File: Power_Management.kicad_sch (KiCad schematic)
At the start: 21 parts

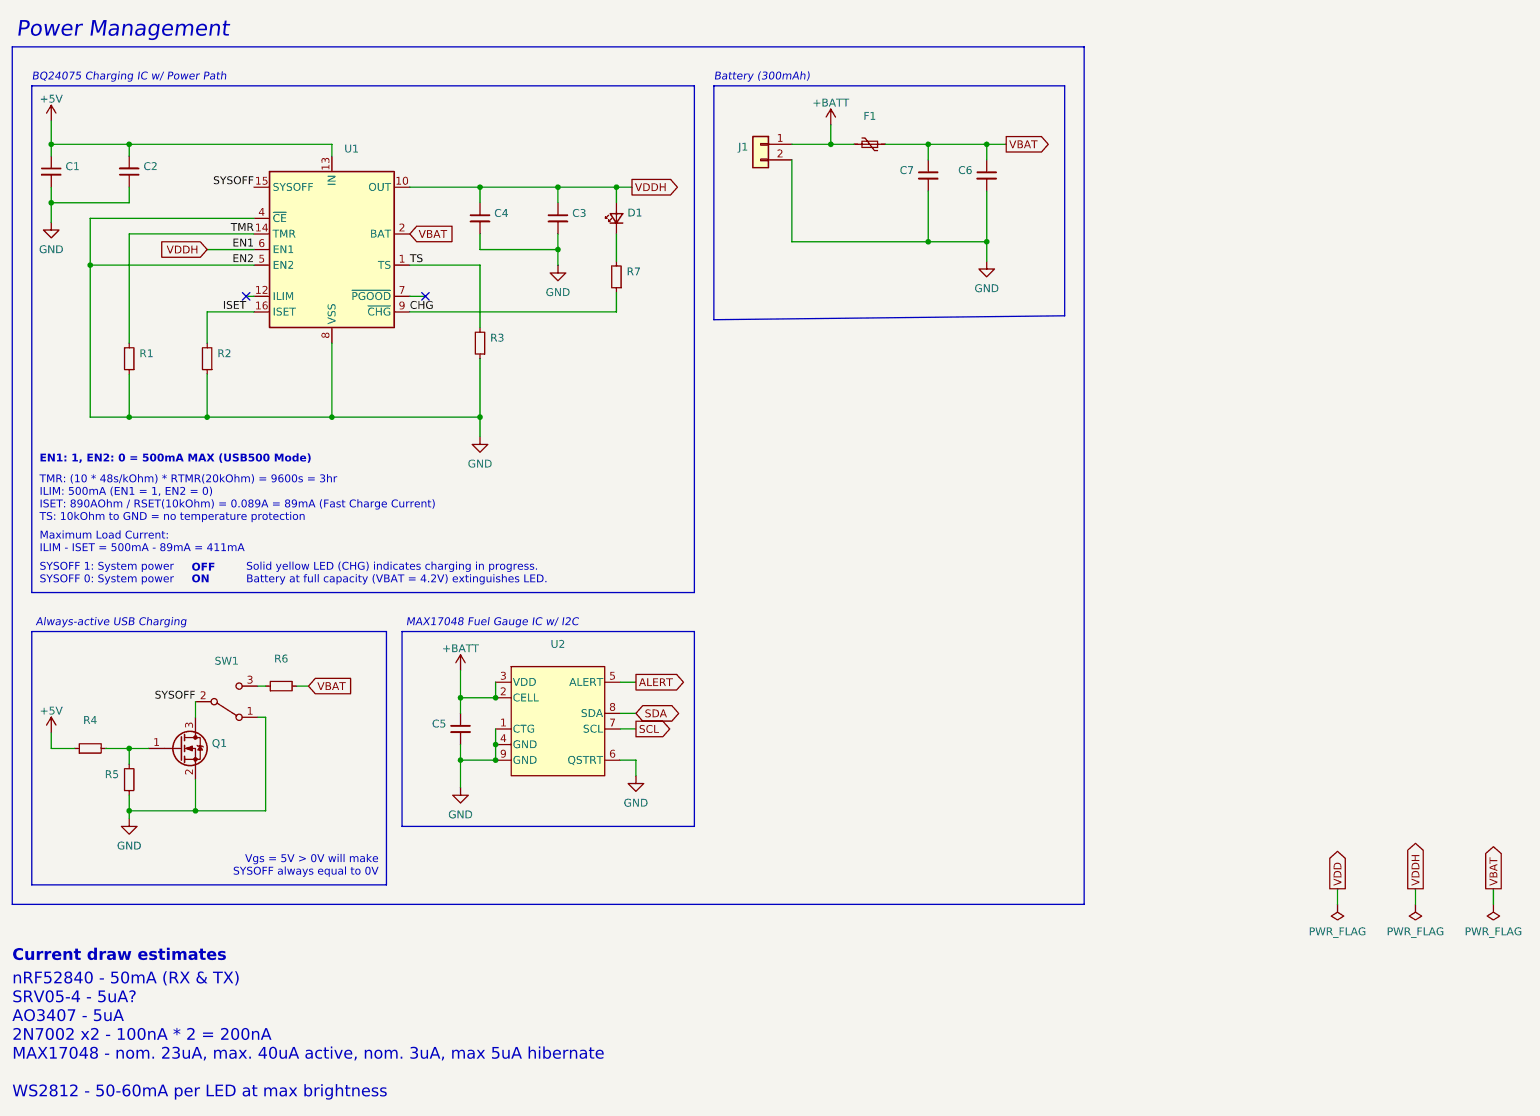
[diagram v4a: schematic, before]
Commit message: feat(pcb): Version 1.0.0
- Change decoupling capacitors from 4.7uF/1uF pairs to both 4.7uF
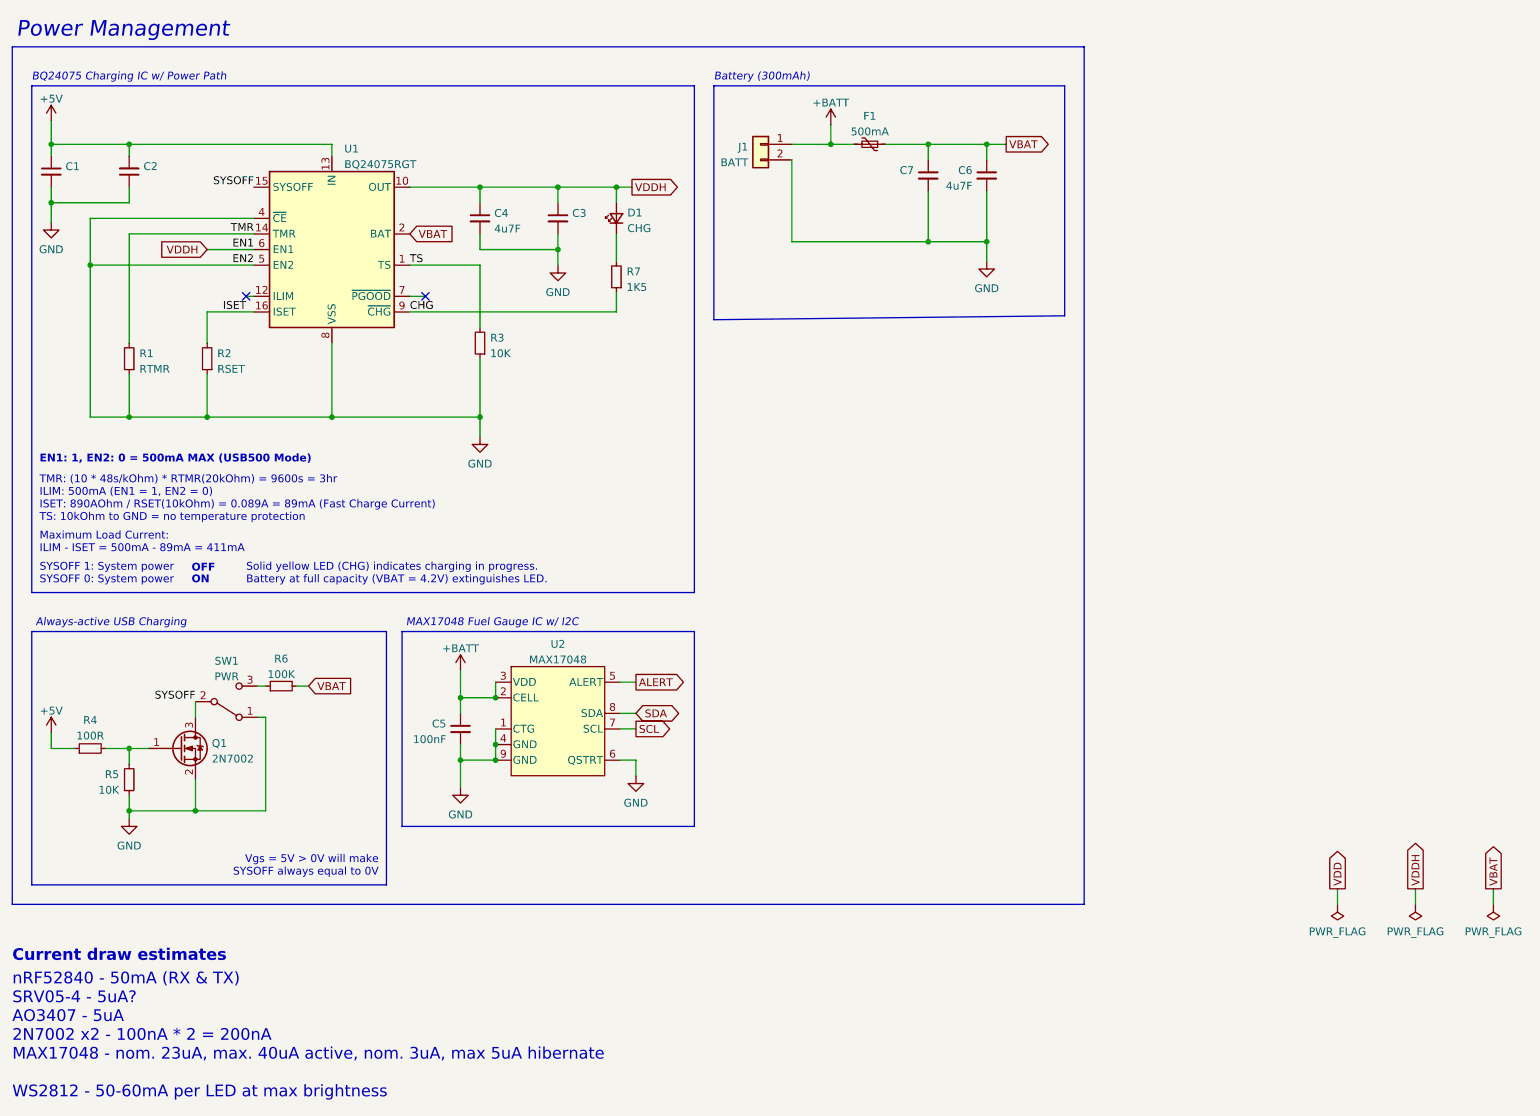
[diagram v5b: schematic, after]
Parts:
- C4, C6: value (none) -> 4u7F; footprint (none) -> Capacitor_SMD:C_0402_1005Metric
- C5: value (none) -> 100nF; footprint (none) -> Capacitor_SMD:C_0402_1005Metric
- D1: value (none) -> CHG; footprint (none) -> Conejo:LED_1206_3216Metric (Reversible)
- F1: value (none) -> 500mA; footprint (none) -> Fuse:Fuse_0603_1608Metric
- J1: value (none) -> BATT; footprint (none) -> Conejo:Battery Header
- Q1: value (none) -> 2N7002; footprint (none) -> Package_TO_SOT_SMD:SOT-23
- R1: value (none) -> RTMR; footprint (none) -> Resistor_SMD:R_0402_1005Metric
- R2: value (none) -> RSET; footprint (none) -> Resistor_SMD:R_0402_1005Metric
- R3, R5: value (none) -> 10K; footprint (none) -> Resistor_SMD:R_0402_1005Metric
- R4: value (none) -> 100R; footprint (none) -> Resistor_SMD:R_0402_1005Metric
- R6: value (none) -> 100K; footprint (none) -> Resistor_SMD:R_0402_1005Metric
- R7: value (none) -> 1K5; footprint (none) -> Resistor_SMD:R_0402_1005Metric
- SW1: value (none) -> PWR; footprint (none) -> Conejo:SW_MSK12C02-HB (Reversible)
- U1: value (none) -> BQ24075RGT; footprint (none) -> Package_DFN_QFN:VQFN-16-1EP_3x3mm_P0.5mm_EP1.6x1.6mm
- U2: value (none) -> MAX17048; footprint (none) -> Package_DFN_QFN:TDFN-8-1EP_2x2mm_P0.5mm_EP0.8x1.2mm
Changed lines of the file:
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@@
       (effects (font (size 1.27 1.27)) (justify left))
     )
-    (property "Value" "" (id 1) (at 45.212 135.0522 0)
-      (effects (font (size 1.27 1.27)) (justify left))
-    )
-    (property "Footprint" "" (id 2) (at 45.085 135.255 0)
+    (property "Value" "2N7002" (id 1) (at 45.212 135.0522 0)
+      (effects (font (size 1.27 1.27)) (justify left))
+    )
+    (property "Footprint" "Package_TO_SOT_SMD:SOT-23" (id 2) (at 45.085 135.255 0)
       (effects (font (size 1.27 1.27) italic) (justify left) hide)
     )
@@
     (in_bom yes) (on_board yes) (fields_autoplaced)
     (property "Reference" "SW1" (id 0) (at 47.625 119.1092 0))
-    (property "Value" "" (id 1) (at 47.625 121.6461 0))
-    (property "Footprint" "" (id 2) (at 47.625 125.73 0)
+    (property "Value" "PWR" (id 1) (at 47.625 121.6461 0))
+    (property "Footprint" "Conejo:SW_MSK12C02-HB (Reversible)" (id 2) (at 47.625 125.73 0)
       (effects (font (size 1.27 1.27)) hide)
     )
@@
       (effects (font (size 1.27 1.27)) (justify left))
     )
-    (property "Value" "" (id 1) (at 169.1259 41.7135 0)
-      (effects (font (size 1.27 1.27)) (justify left))
-    )
-    (property "Footprint" "" (id 2) (at 171.45 40.005 0)
+    (property "Value" "4u7F" (id 1) (at 169.1259 41.7135 0)
+      (effects (font (size 1.27 1.27)) (justify left))
+    )
+    (property "Footprint" "Capacitor_SMD:C_0402_1005Metric" (id 2) (at 171.45 40.005 0)
       (effects (font (size 1.27 1.27)) hide)
     )
@@
     (in_bom yes) (on_board yes) (fields_autoplaced)
     (property "Reference" "R4" (id 0) (at 25.4 128.7612 90))
-    (property "Value" "" (id 1) (at 25.4 131.2981 90))
-    (property "Footprint" "" (id 2) (at 25.4 133.35 0)
+    (property "Value" "100R" (id 1) (at 25.4 131.2981 90))
+    (property "Footprint" "Resistor_SMD:R_0402_1005Metric" (id 2) (at 25.4 133.35 0)
       (effects (font (size 1.27 1.27)) hide)
     )
@@
     (in_bom yes) (on_board yes) (fields_autoplaced)
     (property "Reference" "U2" (id 0) (at 101.6 116.366 0))
-    (property "Value" "" (id 1) (at 101.6 118.9029 0))
-    (property "Footprint" "" (id 2) (at 101.6 128.905 0)
+    (property "Value" "MAX17048" (id 1) (at 101.6 118.9029 0))
+    (property "Footprint" "Package_DFN_QFN:TDFN-8-1EP_2x2mm_P0.5mm_EP0.8x1.2mm" (id 2) (at 101.6 128.905 0)
       (effects (font (size 1.27 1.27)) hide)
     )
@@
       (effects (font (size 1.27 1.27)) (justify right))
     )
-    (property "Value" "" (id 1) (at 112.903 48.6287 90)
-      (effects (font (size 1.27 1.27)) (justify right))
-    )
-    (property "Footprint" "" (id 2) (at 111.125 46.99 90)
+    (property "Value" "CHG" (id 1) (at 112.903 48.6287 90)
+      (effects (font (size 1.27 1.27)) (justify right))
+    )
+    (property "Footprint" "Conejo:LED_1206_3216Metric (Reversible)" (id 2) (at 111.125 46.99 90)
       (effects (font (size 1.27 1.27)) hide)
     )
@@
       (effects (font (size 1.27 1.27)) (justify right))
     )
-    (property "Value" "" (id 1) (at 33.401 71.5522 0)
-      (effects (font (size 1.27 1.27)) (justify right))
-    )
-    (property "Footprint" "" (id 2) (at 31.75 69.85 0)
+    (property "Value" "RTMR" (id 1) (at 33.401 71.5522 0)
+      (effects (font (size 1.27 1.27)) (justify right))
+    )
+    (property "Footprint" "Resistor_SMD:R_0402_1005Metric" (id 2) (at 31.75 69.85 0)
       (effects (font (size 1.27 1.27)) hide)
     )
@@
       (effects (font (size 1.27 1.27)) (justify right))
     )
-    (property "Value" "" (id 1) (at 90.551 69.0122 0)
-      (effects (font (size 1.27 1.27)) (justify right))
-    )
-    (property "Footprint" "" (id 2) (at 88.9 67.31 0)
+    (property "Value" "10K" (id 1) (at 90.551 69.0122 0)
+      (effects (font (size 1.27 1.27)) (justify right))
+    )
+    (property "Footprint" "Resistor_SMD:R_0402_1005Metric" (id 2) (at 88.9 67.31 0)
       (effects (font (size 1.27 1.27)) hide)
     )
@@
     (in_bom yes) (on_board yes) (fields_autoplaced)
     (property "Reference" "F1" (id 0) (at 152.4 30.3362 90))
-    (property "Value" "" (id 1) (at 152.4 32.8731 90))
-    (property "Footprint" "" (id 2) (at 147.32 33.655 0)
+    (property "Value" "500mA" (id 1) (at 152.4 32.8731 90))
+    (property "Footprint" "Fuse:Fuse_0603_1608Metric" (id 2) (at 147.32 33.655 0)
       (effects (font (size 1.27 1.27)) (justify left) hide)
     )
@@
     (in_bom yes) (on_board yes) (fields_autoplaced)
     (property "Reference" "R6" (id 0) (at 56.515 118.7536 90))
-    (property "Value" "" (id 1) (at 56.515 121.2905 90))
-    (property "Footprint" "" (id 2) (at 56.515 123.19 0)
+    (property "Value" "100K" (id 1) (at 56.515 121.2905 90))
+    (property "Footprint" "Resistor_SMD:R_0402_1005Metric" (id 2) (at 56.515 123.19 0)
       (effects (font (size 1.27 1.27)) hide)
     )
@@
       (effects (font (size 1.27 1.27)) (justify left))
     )
-    (property "Value" "" (id 1) (at 66.7894 38.2071 0)
-      (effects (font (size 1.27 1.27)) (justify left))
-    )
-    (property "Footprint" "" (id 2) (at 72.39 66.04 0)
+    (property "Value" "BQ24075RGT" (id 1) (at 66.7894 38.2071 0)
+      (effects (font (size 1.27 1.27)) (justify left))
+    )
+    (property "Footprint" "Package_DFN_QFN:VQFN-16-1EP_3x3mm_P0.5mm_EP1.6x1.6mm" (id 2) (at 72.39 66.04 0)
       (effects (font (size 1.27 1.27)) (justify left) hide)
     )
@@
       (effects (font (size 1.27 1.27)) (justify left))
     )
-    (property "Value" "" (id 1) (at 91.2241 48.6985 0)
-      (effects (font (size 1.27 1.27)) (justify left))
-    )
-    (property "Footprint" "" (id 2) (at 88.9 46.99 0)
+    (property "Value" "4u7F" (id 1) (at 91.2241 48.6985 0)
+      (effects (font (size 1.27 1.27)) (justify left))
+    )
+    (property "Footprint" "Capacitor_SMD:C_0402_1005Metric" (id 2) (at 88.9 46.99 0)
       (effects (font (size 1.27 1.27)) hide)
     )
@@
       (effects (font (size 1.27 1.27)) (justify right))
     )
-    (property "Value" "" (id 1) (at 112.776 58.2172 0)
-      (effects (font (size 1.27 1.27)) (justify right))
-    )
-    (property "Footprint" "" (id 2) (at 111.125 56.515 0)
+    (property "Value" "1K5" (id 1) (at 112.776 58.2172 0)
+      (effects (font (size 1.27 1.27)) (justify right))
+    )
+    (property "Footprint" "Resistor_SMD:R_0402_1005Metric" (id 2) (at 111.125 56.515 0)
       (effects (font (size 1.27 1.27)) hide)
     )
@@
       (effects (font (size 1.27 1.27)) (justify left))
     )
-    (property "Value" "" (id 1) (at 83.4009 131.8835 0)
-      (effects (font (size 1.27 1.27)) (justify left))
-    )
-    (property "Footprint" "" (id 2) (at 85.725 130.175 0)
+    (property "Value" "100nF" (id 1) (at 83.4009 131.8835 0)
+      (effects (font (size 1.27 1.27)) (justify left))
+    )
+    (property "Footprint" "Capacitor_SMD:C_0402_1005Metric" (id 2) (at 85.725 130.175 0)
       (effects (font (size 1.27 1.27)) hide)
     )
@@
       (effects (font (size 1.27 1.27)) (justify left))
     )
-    (property "Value" "" (id 1) (at 132.588 37.8972 0)
-      (effects (font (size 1.27 1.27)) (justify left))
-    )
-    (property "Footprint" "" (id 2) (at 134.62 34.925 0)
+    (property "Value" "BATT" (id 1) (at 132.588 37.8972 0)
+      (effects (font (size 1.27 1.27)) (justify left))
+    )
+    (property "Footprint" "Conejo:Battery Header" (id 2) (at 134.62 34.925 0)
       (effects (font (size 1.27 1.27)) hide)
     )
@@
       (effects (font (size 1.27 1.27)) (justify right))
     )
-    (property "Value" "" (id 1) (at 46.101 71.5522 0)
-      (effects (font (size 1.27 1.27)) (justify right))
-    )
-    (property "Footprint" "" (id 2) (at 44.45 69.85 0)
+    (property "Value" "RSET" (id 1) (at 46.101 71.5522 0)
+      (effects (font (size 1.27 1.27)) (justify right))
+    )
+    (property "Footprint" "Resistor_SMD:R_0402_1005Metric" (id 2) (at 44.45 69.85 0)
       (effects (font (size 1.27 1.27)) hide)
     )
@@
       (effects (font (size 1.27 1.27)) (justify right))
     )
-    (property "Value" "" (id 1) (at 30.099 140.1322 0)
-      (effects (font (size 1.27 1.27)) (justify right))
-    )
-    (property "Footprint" "" (id 2) (at 31.75 138.43 0)
-      (effects (font (size 1.27 1.27)) hide)
-    )
+    (property "Value" "10K" (id 1) (at 30.099 140.1322 0)
+      (effects (font (size 1.27 1.27)) (justify right))
+    )
+    (property "Footprint" "Resistor_SMD:R_0402_1005Metric" (id 2) (at 31.75 138.43 0)
+      (effects (font (size 1.27 1.27)) hide)
+    )
